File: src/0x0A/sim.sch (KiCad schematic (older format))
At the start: 11 parts

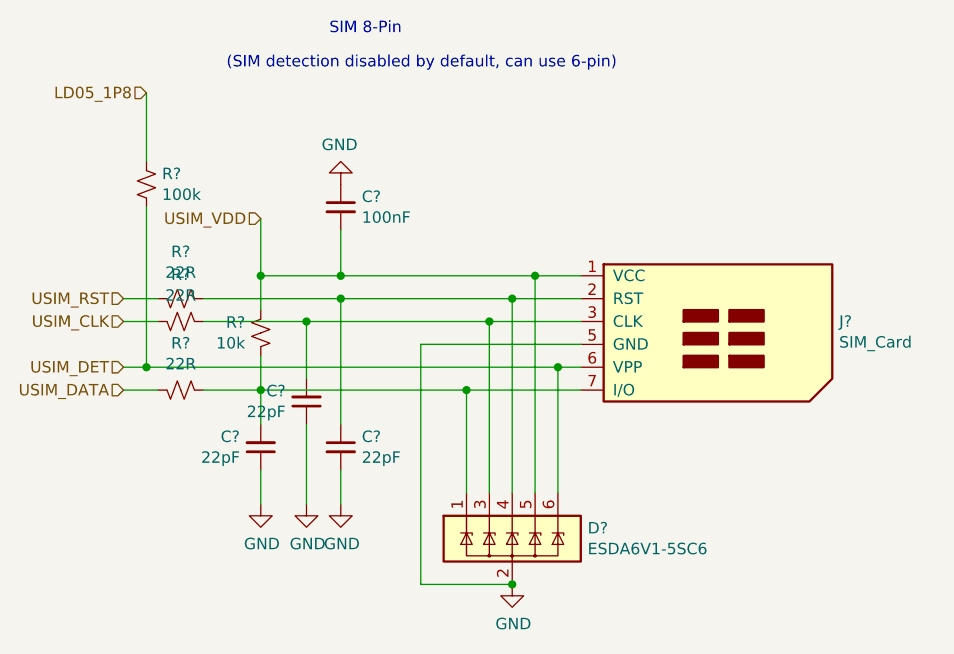
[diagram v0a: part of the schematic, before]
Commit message: new file:   imgs/better.png 	modified:   src/0x0A/0x0A-cache.lib 	modified:   src/0x0A/0x0A.sch 	modified:   src/0x0A/antenna.sch 	modified:   src/0x0A/audio.sch 	modified:   src/0x0A/buttons.sch 	new file:   src/0x0A/cameras.sch 	modified:   src/0x0A/display.sch 	modified:   src/0x0A/gpio.sch 	modified:   src/0x0A/pwr.sch 	modified:   src/0x0A/sensors.sch 	modified:   src/0x0A/sim.sch 	modified:   src/0x0A/uart.sch 	modified:   src/0x0A/usb.sch 	new file:   src/models/body.obj 	new file:   src/models/phone.FCStd 	new file:   src/models/screen.obj
Added 3D models, integrated front & rear cameras, flash light, reformatting & more
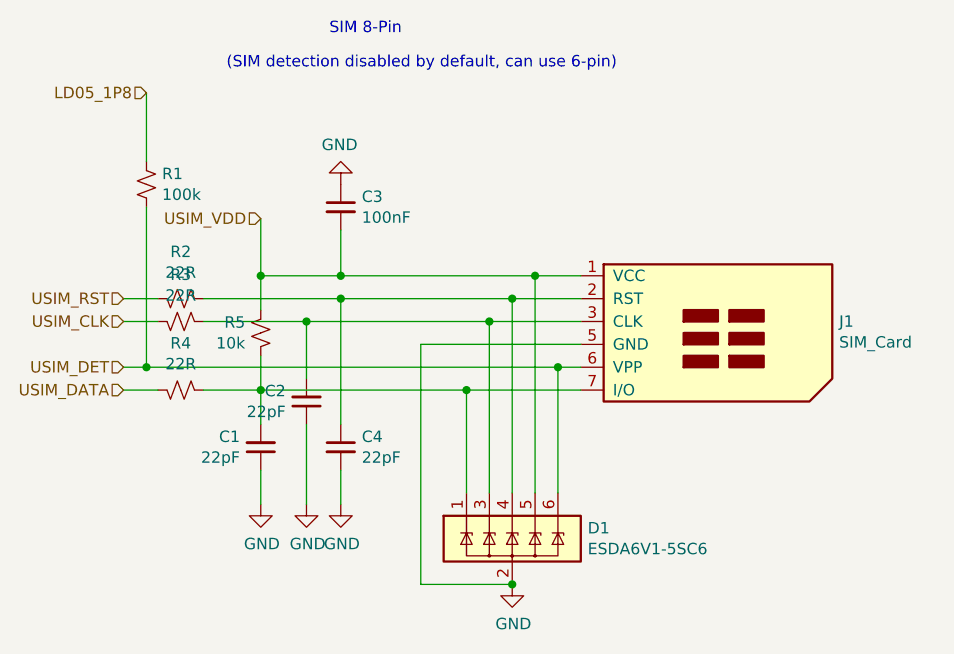
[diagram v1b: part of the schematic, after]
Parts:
- C1, C2, C3, C4: renamed from C?; footprint (none) -> Capacitor_SMD:C_0603_1608Metric
- R1, R2, R3, R4, R5: renamed from R?; footprint (none) -> Resistor_SMD:R_0402_1005Metric
- gave numbers to parts that had none: 2
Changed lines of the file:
@@
 $Descr A4 11693 8268
 encoding utf-8
-Sheet 4 12
+Sheet 3 13
 Title "0x0A SmartPhone"
 Date "2022-09-01"
 Rev "1"
 Comp "HackThisPhone.com"
-Comment1 ""
-Comment2 ""
+Comment1 "Designed By @NoahGWood for"
+Comment2 "uSIM Circuit"
 Comment3 ""
 Comment4 ""
@@
 	3150 2150 3150 3000
 $Comp
-L Power_Protection:ESDA6V1-5SC6 D?
+L Power_Protection:ESDA6V1-5SC6 D1
 U 1 1 632AE17E
 P 3150 3200
-F 0 "D?" H 3480 3246 50  0000 L CNN
+F 0 "D1" H 3480 3246 50  0000 L CNN
 F 1 "ESDA6V1-5SC6" H 3480 3155 50  0000 L CNN
 F 2 "Package_TO_SOT_SMD:SOT-23-6" H 3850 2950 50  0001 C CNN
@@
 $EndComp
 $Comp
-L power:GND #PWR?
+L power:GND #PWR0102
 U 1 1 632AD11A
 P 3150 3400
-F 0 "#PWR?" H 3150 3150 50  0001 C CNN
+F 0 "#PWR0102" H 3150 3150 50  0001 C CNN
 F 1 "GND" H 3155 3227 50  0000 C CNN
 F 2 "" H 3150 3400 50  0001 C CNN
@@
 	1600 2250 1450 2250
 $Comp
-L Device:R_Small_US R?
+L Device:R_Small_US R3
 U 1 1 632A7145
 P 1700 2250
-F 0 "R?" V 1905 2250 50  0000 C CNN
+F 0 "R3" V 1905 2250 50  0000 C CNN
 F 1 "22R" V 1814 2250 50  0000 C CNN
-F 2 "" H 1700 2250 50  0001 C CNN
+F 2 "Resistor_SMD:R_0402_1005Metric" H 1700 2250 50  0001 C CNN
 F 3 "~" H 1700 2250 50  0001 C CNN
 	1    1700 2250
@@
 	1600 2150 1450 2150
 $Comp
-L Device:R_Small_US R?
+L Device:R_Small_US R2
 U 1 1 632A1D5E
 P 1700 2150
-F 0 "R?" V 1905 2150 50  0000 C CNN
+F 0 "R2" V 1905 2150 50  0000 C CNN
 F 1 "22R" V 1814 2150 50  0000 C CNN
-F 2 "" H 1700 2150 50  0001 C CNN
+F 2 "Resistor_SMD:R_0402_1005Metric" H 1700 2150 50  0001 C CNN
 F 3 "~" H 1700 2150 50  0001 C CNN
 	1    1700 2150
@@
 	2400 3050 2400 2900
 $Comp
-L power:GND #PWR?
+L power:GND #PWR0103
 U 1 1 632A0BFE
 P 2400 3050
-F 0 "#PWR?" H 2400 2800 50  0001 C CNN
+F 0 "#PWR0103" H 2400 2800 50  0001 C CNN
 F 1 "GND" H 2405 2877 50  0000 C CNN
 F 2 "" H 2400 3050 50  0001 C CNN
@@
 	2250 3050 2250 2700
 $Comp
-L power:GND #PWR?
+L power:GND #PWR0104
 U 1 1 632A0692
 P 2250 3050
-F 0 "#PWR?" H 2250 2800 50  0001 C CNN
+F 0 "#PWR0104" H 2250 2800 50  0001 C CNN
 F 1 "GND" H 2255 2877 50  0000 C CNN
 F 2 "" H 2250 3050 50  0001 C CNN
@@
 	2250 2500 2250 2250
 $Comp
-L Device:C_Small C?
+L Device:C_Small C2
 U 1 1 6329AA55
 P 2250 2600
-F 0 "C?" H 2159 2554 50  0000 R CNN
+F 0 "C2" H 2159 2554 50  0000 R CNN
 F 1 "22pF" H 2159 2645 50  0000 R CNN
-F 2 "" H 2250 2600 50  0001 C CNN
+F 2 "Capacitor_SMD:C_0603_1608Metric" H 2250 2600 50  0001 C CNN
 F 3 "~" H 2250 2600 50  0001 C CNN
 	1    2250 2600
@@
 $EndComp
 $Comp
-L Device:C_Small C?
+L Device:C_Small C4
 U 1 1 6329A846
 P 2400 2800
-F 0 "C?" H 2492 2846 50  0000 L CNN
+F 0 "C4" H 2492 2846 50  0000 L CNN
 F 1 "22pF" H 2492 2755 50  0000 L CNN
-F 2 "" H 2400 2800 50  0001 C CNN
+F 2 "Capacitor_SMD:C_0603_1608Metric" H 2400 2800 50  0001 C CNN
 F 3 "~" H 2400 2800 50  0001 C CNN
 	1    2400 2800
@@
 	2050 2550 2050 2700
 $Comp
-L power:GND #PWR?
+L power:GND #PWR0105
 U 1 1 63296594
 P 2050 3050
-F 0 "#PWR?" H 2050 2800 50  0001 C CNN
+F 0 "#PWR0105" H 2050 2800 50  0001 C CNN
 F 1 "GND" H 2055 2877 50  0000 C CNN
 F 2 "" H 2050 3050 50  0001 C CNN
@@
 $EndComp
 $Comp
-L Device:C_Small C?
+L Device:C_Small C1
 U 1 1 632960F3
 P 2050 2800
-F 0 "C?" H 1959 2754 50  0000 R CNN
+F 0 "C1" H 1959 2754 50  0000 R CNN
 F 1 "22pF" H 1959 2845 50  0000 R CNN
-F 2 "" H 2050 2800 50  0001 C CNN
+F 2 "Capacitor_SMD:C_0603_1608Metric" H 2050 2800 50  0001 C CNN
 F 3 "~" H 2050 2800 50  0001 C CNN
 	1    2050 2800
@@
 	1600 2550 1450 2550
 $Comp
-L Device:R_Small_US R?
+L Device:R_Small_US R4
 U 1 1 63294C66
 P 1700 2550
-F 0 "R?" V 1905 2550 50  0000 C CNN
+F 0 "R4" V 1905 2550 50  0000 C CNN
 F 1 "22R" V 1814 2550 50  0000 C CNN
-F 2 "" H 1700 2550 50  0001 C CNN
+F 2 "Resistor_SMD:R_0402_1005Metric" H 1700 2550 50  0001 C CNN
 F 3 "~" H 1700 2550 50  0001 C CNN
 	1    1700 2550
@@
 	2050 2400 2050 2550
 $Comp
-L Device:R_Small_US R?
+L Device:R_Small_US R5
 U 1 1 63286BBD
 P 2050 2300
-F 0 "R?" H 2118 2346 50  0000 L CNN
+F 0 "R5" H 2118 2346 50  0000 L CNN
 F 1 "10k" H 2118 2255 50  0000 L CNN
-F 2 "" H 2050 2300 50  0001 C CNN
+F 2 "Resistor_SMD:R_0402_1005Metric" H 2050 2300 50  0001 C CNN
 F 3 "~" H 2050 2300 50  0001 C CNN
 	1    2050 2300
@@
 	2400 2050 2400 1850
 $Comp
-L power:GND #PWR?
+L power:GND #PWR0106
 U 1 1 63288604
 P 2400 1650
-F 0 "#PWR?" H 2400 1400 50  0001 C CNN
+F 0 "#PWR0106" H 2400 1400 50  0001 C CNN
 F 1 "GND" H 2405 1477 50  0000 C CNN
 F 2 "" H 2400 1650 50  0001 C CNN
@@
 USIM_DET
 $Comp
-L Device:C_Small C?
+L Device:C_Small C3
 U 1 1 63286ECA
 P 2400 1750
-F 0 "C?" H 2492 1796 50  0000 L CNN
+F 0 "C3" H 2492 1796 50  0000 L CNN
 F 1 "100nF" H 2492 1705 50  0000 L CNN
-F 2 "" H 2400 1750 50  0001 C CNN
+F 2 "Capacitor_SMD:C_0603_1608Metric" H 2400 1750 50  0001 C CNN
 F 3 "~" H 2400 1750 50  0001 C CNN
 	1    2400 1750
@@
 $EndComp
 $Comp
-L Device:R_Small_US R?
+L Device:R_Small_US R1
 U 1 1 63286AF0
 P 1550 1650
-F 0 "R?" H 1618 1696 50  0000 L CNN
+F 0 "R1" H 1618 1696 50  0000 L CNN
 F 1 "100k" H 1618 1605 50  0000 L CNN
-F 2 "" H 1550 1650 50  0001 C CNN
+F 2 "Resistor_SMD:R_0402_1005Metric" H 1550 1650 50  0001 C CNN
 F 3 "~" H 1550 1650 50  0001 C CNN
 	1    1550 1650
@@
 $EndComp
 $Comp
-L Connector:SIM_Card J?
+L Connector:SIM_Card J1
 U 1 1 63286267
 P 3950 2350
-F 0 "J?" H 4580 2450 50  0000 L CNN
+F 0 "J1" H 4580 2450 50  0000 L CNN
 F 1 "SIM_Card" H 4580 2359 50  0000 L CNN
 F 2 "" H 3950 2700 50  0001 C CNN

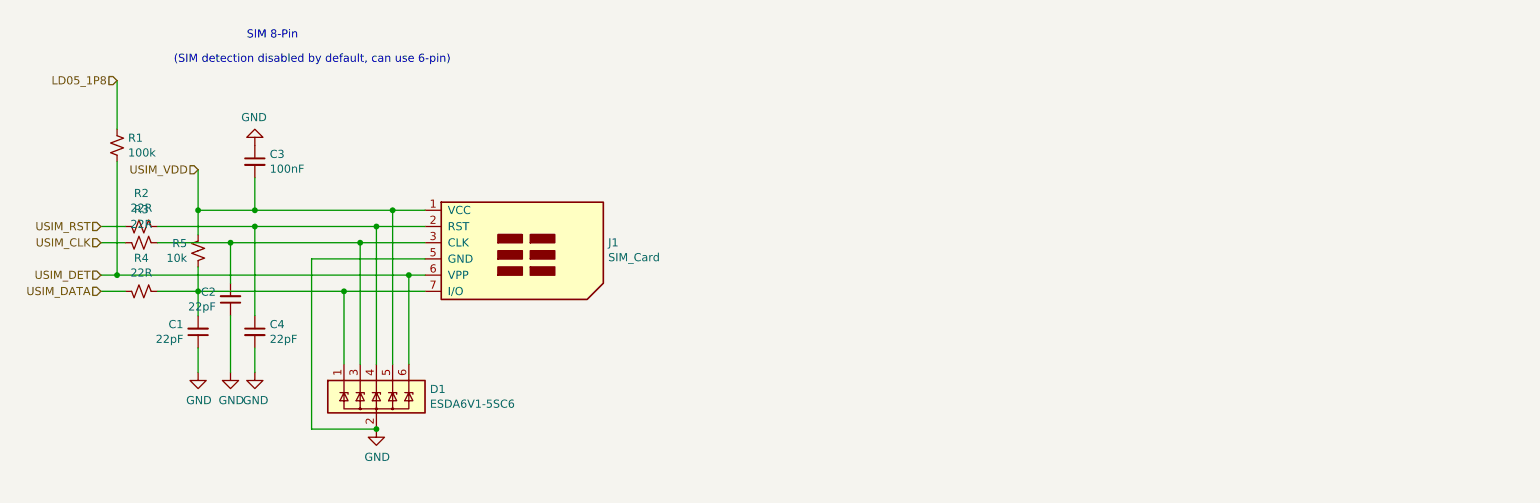
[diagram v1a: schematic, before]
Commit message: Updated schematics, started working on board layout
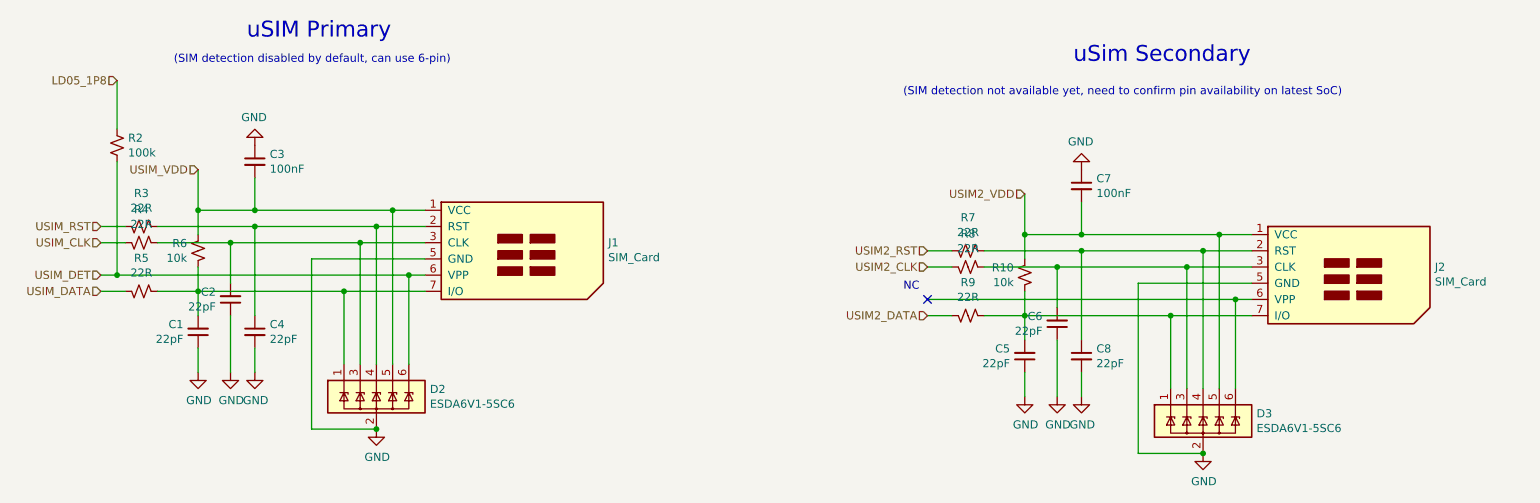
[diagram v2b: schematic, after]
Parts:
- added C5, C6, C8: 22pF, Capacitor_SMD:C_0402_1005Metric, symbol Device:C_Small
- added C7: 100nF, Capacitor_SMD:C_0402_1005Metric, symbol Device:C_Small
- added D3: ESDA6V1-5SC6, Package_TO_SOT_SMD:SOT-23-6, symbol Power_Protection:ESDA6V1-5SC6
- added J2: SIM_Card, 0x0A:SIM-002-P6, symbol Connector:SIM_Card
- added R10: 10k, Resistor_SMD:R_0402_1005Metric, symbol Device:R_Small_US
- added R7, R8, R9: 22R, Resistor_SMD:R_0402_1005Metric, symbol Device:R_Small_US
- C1, C2, C4: footprint Capacitor_SMD:C_0603_1608Metric -> Capacitor_SMD:C_0402_1005Metric; LCSC Part # (none) -> C1555
- C3: footprint Capacitor_SMD:C_0603_1608Metric -> Capacitor_SMD:C_0402_1005Metric; LCSC Part # (none) -> C307331
- J1: footprint (none) -> 0x0A:SIM-002-P6; LCSC Part # (none) -> C390900; MANUFACTURER (none) -> SOFNG
- renumbered D1 to D2, R1 to R2, R2 to R3, R3 to R4, R4 to R5, R5 to R6
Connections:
- net GND: now also C5.1, C6.1, C7.1, C8.2, D3.2 (GND), J2.5 (GND)
- new net: C5.2, D3.1 (IO1), J2.7 (I/O), R10.2, R9.1
- new net: C6.2, D3.3 (IO2), J2.3 (CLK), R8.1
- new net: C8.1, D3.4 (IO3), J2.2 (RST), R7.1
- new net: D3.6 (IO5), J2.6 (VPP)
- new net USIM2_CLK: R8.2
- new net USIM2_DATA: R9.2
- new net USIM2_RST: R7.2
- new net USIM2_VDD: C7.2, D3.5 (IO4), J2.1 (VCC), R10.1
- no-connect marks 0 -> 1
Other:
- note added: "(SIM detection not available yet, need to confirm pin availability on latest SoC)"
- note added: "NC"
- note added: "uSIM Primary"
- note added: "uSim Secondary"
- note removed: "SIM 8-Pin"
